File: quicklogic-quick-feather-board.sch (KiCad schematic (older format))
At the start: 28 parts, among them IC1 EOS-S3, J5 0473460001, U1 TPS62821DLCR, U2 MCP73831T-2ACI_OT, U3 MX25U6435FZNI-10G, X1 ECS-_327-12_5-34B-TR

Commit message: Changed flash memory, connected missing nets, cleanup
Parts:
- removed R9: R_10k_0402, antmicro-footprints:0402-res, symbol antmicroResistors0402:R_10k_0402
- removed U3: MX25U6435FZNI-10G, antmicro-footprints:DFN-8-1EP_6x5mm_P1.27mm_EP4x3.4mm, symbol quicklogic-quick-feather-board-rescue:MX25U6435FZNI-10G-antmicroMemory
- added R11, R7: R_22R_0402, antmicro-footprints:0402-res, symbol antmicroResistors0402:R_22R_0402
- added R12: R_10k_0402, antmicro-footprints:0402-res, symbol antmicroResistors0402:R_10k_0402
- added R9: R_1k5_0402, antmicro-footprints:0402-res, symbol antmicroResistors0402:R_1k5_0402
- added U3: GD25Q16CWIGR, antmicro-footprints:GD25Q16CWIG, symbol antmicroMemory:GD25Q16CWIGR
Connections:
- net labels added: PU_CTRL_USBP, SPI_HOLD, SPI_WP
- net labels removed: 1V8_SYS, EOS_VDD, IO23, IO28, IO29, SPI_MASTER_MISO, SPI_MASTER_MOSI, SPI_MASTER_SCK, SPI_MASTER_SS
- wire segments 110 -> 119
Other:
- note added: "Battery charger"
- note added: "EOS S3 FPGA"
- note added: "Flash memory"
- note added: "Supply"
- note added: "USB"
- note added: "Within same package this Flash can be replaced with \n64Mb one (GD25Q64CWIGR)"
- note removed: "TODO: connect SPI flash, add voltage level shifting if necessary (and pullups)"
- note removed: "TODO: connect to power supply source"
- note removed: "TODO: decide if we want to have 1v8 or 3v3 power supply for EOS (flash requires 1v8)"
- moved on the sheet: C1, C2, C3, C4, C5, C6, C7, D1, D2, J5, L1, R1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

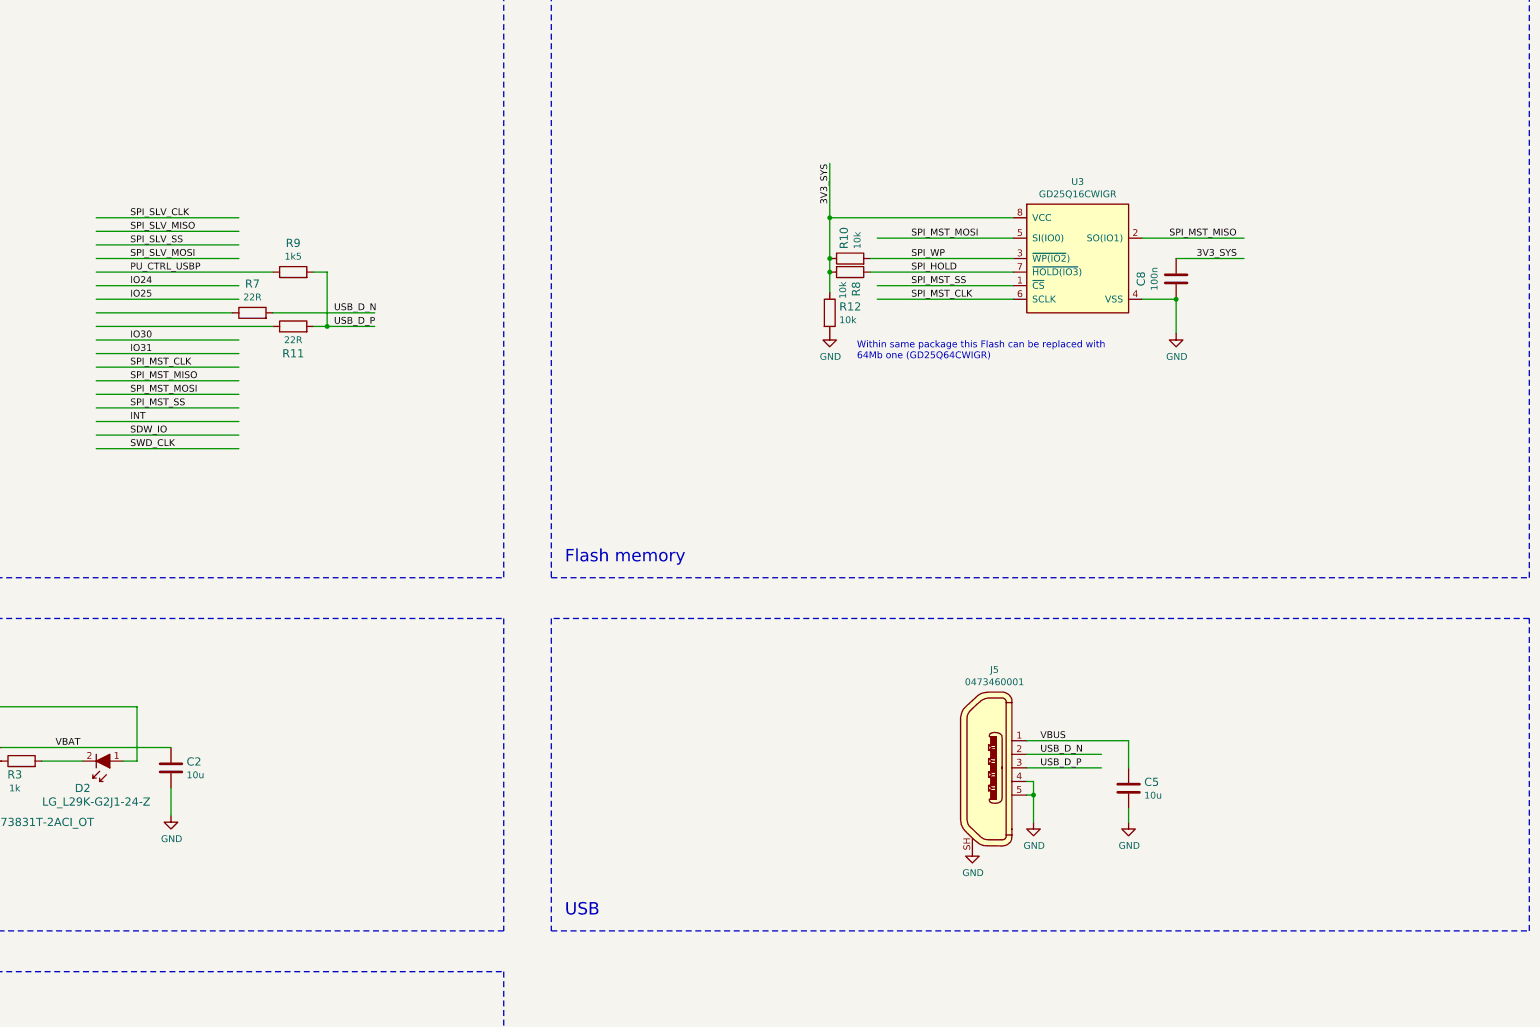
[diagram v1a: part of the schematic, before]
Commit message: Added IM69D130 microphone to schematics
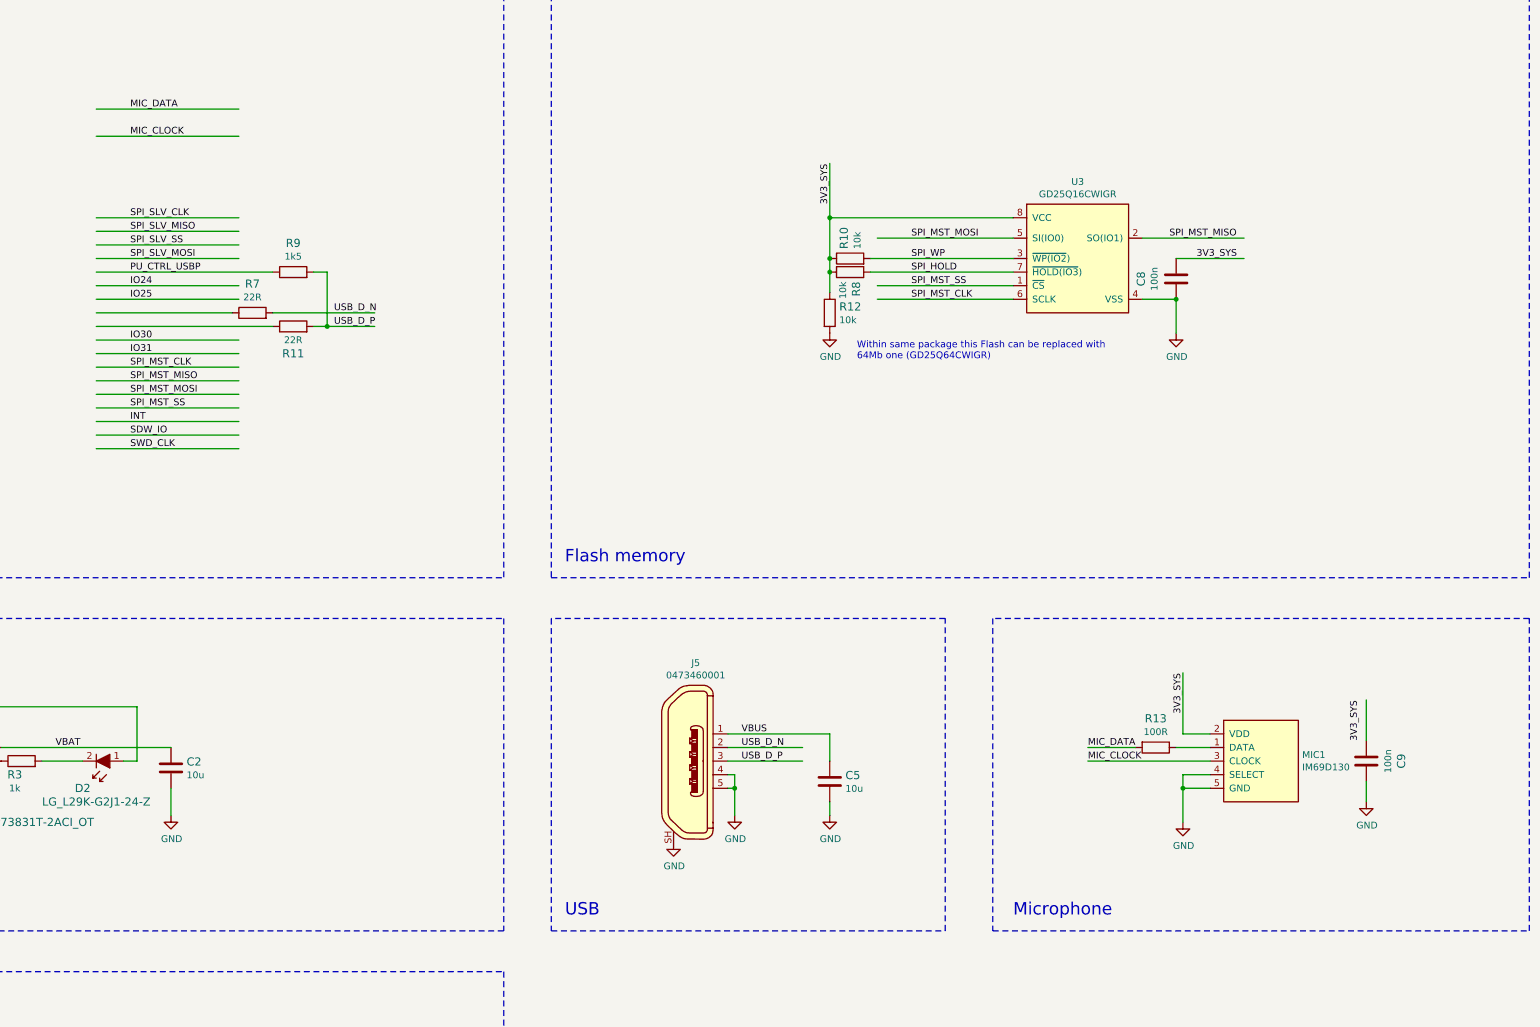
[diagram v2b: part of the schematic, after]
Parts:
- added C9: C_100n_0402_6V3, antmicro-footprints:0402-cap, symbol antmicroCapacitors0402:C_100n_0402_6V3
- added MIC1: IM69D130, antmicro-footprints:IM69D130, symbol antmicroMicrophones:IM69D130
- added R13: R_100R_0402, antmicro-footprints:0402-res, symbol antmicroResistors0402:R_100R_0402
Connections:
- net labels added: MIC_CLOCK, MIC_DATA
- wire segments 119 -> 132
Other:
- note added: "Microphone"
- moved on the sheet: C5, J5
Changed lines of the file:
@@
 L antmicroUSBDVIHDMIConnectors:0473460001 J5
 U 1 1 5DB1F3A2
-P 11800 6600
-F 0 "J5" H 11863 7323 50  0000 C CNN
-F 1 "0473460001" H 11863 7232 50  0000 C CNN
-F 2 "antmicro-footprints:USB_Micro_B_Female_0473460001" H 12000 6800 60  0001 L CNN
-F 3 "https://www.molex.com/pdm_docs/sd/473460001_sd.pdf" H 12000 6900 60  0001 L CNN
-F 4 "0473460001" H 12000 7100 60  0001 L CNN "MPN"
-F 5 "Molex" H 12000 7700 60  0001 L CNN "Manufacturer"
-	1    11800 6600
-	1    0    0    -1
-$EndComp
-Wire Wire Line
-	12100 6500 12650 6500
-Wire Wire Line
-	12100 6600 12650 6600
-Wire Wire Line
-	12100 6700 12150 6700
-Wire Wire Line
-	12150 6700 12150 6800
-Wire Wire Line
-	12150 6800 12100 6800
-Wire Wire Line
-	12150 6800 12150 7000
+P 9600 6550
+F 0 "J5" H 9663 7273 50  0000 C CNN
+F 1 "0473460001" H 9663 7182 50  0000 C CNN
+F 2 "antmicro-footprints:USB_Micro_B_Female_0473460001" H 9800 6750 60  0001 L CNN
+F 3 "https://www.molex.com/pdm_docs/sd/473460001_sd.pdf" H 9800 6850 60  0001 L CNN
+F 4 "0473460001" H 9800 7050 60  0001 L CNN "MPN"
+F 5 "Molex" H 9800 7650 60  0001 L CNN "Manufacturer"
+	1    9600 6550
+	1    0    0    -1
+$EndComp
+Wire Wire Line
+	9900 6450 10450 6450
+Wire Wire Line
+	9900 6550 10450 6550
+Wire Wire Line
+	9900 6650 9950 6650
+Wire Wire Line
+	9950 6650 9950 6750
+Wire Wire Line
+	9950 6750 9900 6750
+Wire Wire Line
+	9950 6750 9950 6950
 $Comp
 L power:GND #PWR011
 U 1 1 5DCF0111
-P 12150 7000
-F 0 "#PWR011" H 12150 6750 50  0001 C CNN
-F 1 "GND" H 12155 6827 50  0000 C CNN
-F 2 "" H 12150 7000 50  0001 C CNN
-F 3 "" H 12150 7000 50  0001 C CNN
-	1    12150 7000
-	1    0    0    -1
-$EndComp
-Text Label 12200 6400 0    50   ~ 0
+P 9950 6950
+F 0 "#PWR011" H 9950 6700 50  0001 C CNN
+F 1 "GND" H 9955 6777 50  0000 C CNN
+F 2 "" H 9950 6950 50  0001 C CNN
+F 3 "" H 9950 6950 50  0001 C CNN
+	1    9950 6950
+	1    0    0    -1
+$EndComp
+Text Label 10000 6350 0    50   ~ 0
 VBUS
-Text Label 12200 6600 0    50   ~ 0
+Text Label 10000 6550 0    50   ~ 0
 USB_D_P
-Text Label 12200 6500 0    50   ~ 0
+Text Label 10000 6450 0    50   ~ 0
 USB_D_N
-Connection ~ 12150 6800
+Connection ~ 9950 6750
 $Comp
 L power:GND #PWR0101
 U 1 1 5DE8E3C8
-P 11700 7200
-F 0 "#PWR0101" H 11700 6950 50  0001 C CNN
-F 1 "GND" H 11705 7027 50  0000 C CNN
-F 2 "" H 11700 7200 50  0001 C CNN
-F 3 "" H 11700 7200 50  0001 C CNN
-	1    11700 7200
+P 9500 7150
+F 0 "#PWR0101" H 9500 6900 50  0001 C CNN
+F 1 "GND" H 9505 6977 50  0000 C CNN
+F 2 "" H 9500 7150 50  0001 C CNN
+F 3 "" H 9500 7150 50  0001 C CNN
+	1    9500 7150
 	1    0    0    -1
 $EndComp
@@
 L antmicroCapacitors0603:C_10u_0603 C5
 U 1 1 5DC240D8
-P 12850 6750
-F 0 "C5" H 12965 6795 60  0000 L CNN
-F 1 "C_10u_0603" H 12850 6600 60  0001 C CNN
-F 2 "antmicro-footprints:0603-cap" H 13050 6950 60  0001 L CNN
-F 3 "" H 12850 6750 50  0001 C CNN
-F 4 "AVX" H 13050 7150 60  0001 L CNN "Manufacturer"
-F 5 "06036D106MAT2A" H 13050 7050 60  0001 L CNN "MPN"
-F 6 "10u" H 12965 6697 50  0000 L CNN "Val"
-	1    12850 6750
-	1    0    0    -1
-$EndComp
-Wire Wire Line
-	12850 6400 12850 6600
-Wire Wire Line
-	12100 6400 12850 6400
+P 10650 6700
+F 0 "C5" H 10765 6745 60  0000 L CNN
+F 1 "C_10u_0603" H 10650 6550 60  0001 C CNN
+F 2 "antmicro-footprints:0603-cap" H 10850 6900 60  0001 L CNN
+F 3 "" H 10650 6700 50  0001 C CNN
+F 4 "AVX" H 10850 7100 60  0001 L CNN "Manufacturer"
+F 5 "06036D106MAT2A" H 10850 7000 60  0001 L CNN "MPN"
+F 6 "10u" H 10765 6647 50  0000 L CNN "Val"
+	1    10650 6700
+	1    0    0    -1
+$EndComp
+Wire Wire Line
+	10650 6350 10650 6550
+Wire Wire Line
+	9900 6350 10650 6350
 $Comp
 L power:GND #PWR0109
 U 1 1 5DC24A74
-P 12850 7000
-F 0 "#PWR0109" H 12850 6750 50  0001 C CNN
-F 1 "GND" H 12855 6827 50  0000 C CNN
-F 2 "" H 12850 7000 50  0001 C CNN
-F 3 "" H 12850 7000 50  0001 C CNN
-	1    12850 7000
-	1    0    0    -1
-$EndComp
-Wire Wire Line
-	12850 6900 12850 7000
+P 10650 6950
+F 0 "#PWR0109" H 10650 6700 50  0001 C CNN
+F 1 "GND" H 10655 6777 50  0000 C CNN
+F 2 "" H 10650 6950 50  0001 C CNN
+F 3 "" H 10650 6950 50  0001 C CNN
+	1    10650 6950
+	1    0    0    -1
+$EndComp
+Wire Wire Line
+	10650 6850 10650 6950
 $Comp
 L antmicroDiodesRectifiersSingle:MBR0520LT1G D1
@@
 	8600 5500 8600 7800
 Wire Notes Line
-	8600 7800 15800 7800
-Wire Notes Line
-	15800 7800 15800 5500
-Wire Notes Line
-	15800 5500 8600 5500
+	8600 7800 11500 7800
+Wire Notes Line
+	11500 7800 11500 5500
+Wire Notes Line
+	11500 5500 8600 5500
 Text Label 2200 1550 0    50   ~ 0
 3V3_SYS
@@
 Text Notes 8700 7700 0    91   ~ 0
 USB
+Wire Notes Line
+	11850 5500 11850 7800
+Wire Notes Line
+	11850 7800 15800 7800
+Wire Notes Line
+	15800 7800 15800 5500
+Wire Notes Line
+	15800 5500 11850 5500
+$Comp
+L antmicroMicrophones:IM69D130 MIC1
+U 1 1 5DDA20C5
+P 13550 6250
+F 0 "MIC1" H 14128 5996 50  0000 L CNN
+F 1 "IM69D130" H 14128 5905 50  0000 L CNN
+F 2 "antmicro-footprints:IM69D130" H 13550 6300 50  0001 C CNN
+F 3 "https://www.infineon.com/dgdl/Infineon-IM69D130-DS-v01_00-EN.pdf?fileId=5546d462602a9dc801607a0e46511a2e" H 14000 5600 50  0001 C CNN
+	1    13550 6250
+	1    0    0    -1
+$EndComp
+Wire Wire Line
+	13450 6350 13250 6350
+Wire Wire Line
+	13250 6350 13250 5900
+Wire Wire Line
+	13450 6750 13250 6750
+Wire Wire Line
+	13250 6750 13250 7000
+$Comp
+L power:GND #PWR04
+U 1 1 5DDAB4E6
+P 13250 7000
+F 0 "#PWR04" H 13250 6750 50  0001 C CNN
+F 1 "GND" H 13255 6827 50  0000 C CNN
+F 2 "" H 13250 7000 50  0001 C CNN
+F 3 "" H 13250 7000 50  0001 C CNN
+	1    13250 7000
+	1    0    0    -1
+$EndComp
+Wire Wire Line
+	13450 6450 13200 6450
+Wire Wire Line
+	13450 6550 12550 6550
+Wire Wire Line
+	13450 6650 13250 6650
+$Comp
+L antmicroResistors0402:R_100R_0402 R13
+U 1 1 5DDB9D20
+P 13050 6450
+F 0 "R13" H 13050 6237 60  0000 C CNN
+F 1 "R_100R_0402" H 13050 6300 60  0001 C CNN
+F 2 "antmicro-footprints:0402-res" H 13250 6650 60  0001 L CNN
+F 3 "" H 13050 6450 50  0001 C CNN
+F 4 "BOURNS" H 13250 6850 60  0001 L CNN "Manufacturer"
+F 5 "CR0402-FX-1000GLF" H 13250 6750 60  0001 L CNN "MPN"
+F 6 "100R" H 13050 6335 50  0000 C CNN "Val"
+	1    13050 6450
+	-1   0    0    1
+$EndComp
+Wire Wire Line
+	12900 6450 12550 6450
+Wire Wire Line
+	13250 6650 13250 6750
+Connection ~ 13250 6750
+Text Label 13250 6200 1    50   ~ 0
+3V3_SYS
+Text Label 12550 6450 0    50   ~ 0
+MIC_DATA
+Text Label 12550 6550 0    50   ~ 0
+MIC_CLOCK
+Text Notes 12000 7700 0    91   ~ 0
+Microphone
+$Comp
+L antmicroCapacitors0402:C_100n_0402_6V3 C9
+U 1 1 5DDE16B2
+P 14600 6550
+F 0 "C9" V 14342 6550 60  0000 C CNN
+F 1 "C_100n_0402_6V3" H 14600 6400 60  0001 C CNN
+F 2 "antmicro-footprints:0402-cap" H 14800 6750 60  0001 L CNN
+F 3 "" H 14600 6550 50  0001 C CNN
+F 4 "Walsin" H 14800 6950 60  0001 L CNN "Manufacturer"
+F 5 "0402X104K6R3CT" H 14800 6850 60  0001 L CNN "MPN"
+F 6 "100n" V 14440 6550 50  0000 C CNN "Val"
+	1    14600 6550
+	-1   0    0    1
+$EndComp
+Text Label 14550 6400 1    50   ~ 0
+3V3_SYS
+Wire Wire Line
+	14600 6100 14600 6400
+Wire Wire Line
+	14600 6700 14600 6850
+$Comp
+L power:GND #PWR05
+U 1 1 5DDF05E4
+P 14600 6850
+F 0 "#PWR05" H 14600 6600 50  0001 C CNN
+F 1 "GND" H 14605 6677 50  0000 C CNN
+F 2 "" H 14600 6850 50  0001 C CNN
+F 3 "" H 14600 6850 50  0001 C CNN
+	1    14600 6850
+	1    0    0    -1
+$EndComp
+Text Label 5500 1750 0    50   ~ 0
+MIC_DATA
+Text Label 5500 1950 0    50   ~ 0
+MIC_CLOCK
+Wire Wire Line
+	5250 1750 6300 1750
+Wire Wire Line
+	5250 1950 6300 1950
 $EndSCHEMATC

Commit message: Added TVS for USB
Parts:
- added D3: TPD2EUSB30DRTR, antmicro-footprints:SOT-3, symbol antmicroTVSDiodes:TPD2EUSB30DRTR
- U3: symbol antmicroMemory:GD25Q16CWIGR -> quicklogic-quick-feather-board-rescue:GD25Q16CWIGR-antmicroMemory
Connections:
- wire segments 132 -> 138
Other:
- moved on the sheet: C5, J5
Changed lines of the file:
@@
 EESchema Schematic File Version 4
 LIBS:quicklogic-quick-feather-board-cache
-EELAYER 26 0
+EELAYER 30 0
 EELAYER END
 $Descr A3 16535 11693
@@
 L antmicroUSBDVIHDMIConnectors:0473460001 J5
 U 1 1 5DB1F3A2
-P 9600 6550
-F 0 "J5" H 9663 7273 50  0000 C CNN
-F 1 "0473460001" H 9663 7182 50  0000 C CNN
-F 2 "antmicro-footprints:USB_Micro_B_Female_0473460001" H 9800 6750 60  0001 L CNN
-F 3 "https://www.molex.com/pdm_docs/sd/473460001_sd.pdf" H 9800 6850 60  0001 L CNN
-F 4 "0473460001" H 9800 7050 60  0001 L CNN "MPN"
-F 5 "Molex" H 9800 7650 60  0001 L CNN "Manufacturer"
-	1    9600 6550
-	1    0    0    -1
-$EndComp
-Wire Wire Line
-	9900 6450 10450 6450
-Wire Wire Line
-	9900 6550 10450 6550
-Wire Wire Line
-	9900 6650 9950 6650
-Wire Wire Line
-	9950 6650 9950 6750
-Wire Wire Line
-	9950 6750 9900 6750
-Wire Wire Line
-	9950 6750 9950 6950
+P 9000 6550
+F 0 "J5" H 9063 7273 50  0000 C CNN
+F 1 "0473460001" H 9063 7182 50  0000 C CNN
+F 2 "antmicro-footprints:USB_Micro_B_Female_0473460001" H 9200 6750 60  0001 L CNN
+F 3 "https://www.molex.com/pdm_docs/sd/473460001_sd.pdf" H 9200 6850 60  0001 L CNN
+F 4 "0473460001" H 9200 7050 60  0001 L CNN "MPN"
+F 5 "Molex" H 9200 7650 60  0001 L CNN "Manufacturer"
+	1    9000 6550
+	1    0    0    -1
+$EndComp
+Wire Wire Line
+	9300 6650 9350 6650
+Wire Wire Line
+	9350 6650 9350 6750
+Wire Wire Line
+	9350 6750 9300 6750
+Wire Wire Line
+	9350 6750 9350 6950
 $Comp
 L power:GND #PWR011
 U 1 1 5DCF0111
-P 9950 6950
-F 0 "#PWR011" H 9950 6700 50  0001 C CNN
-F 1 "GND" H 9955 6777 50  0000 C CNN
-F 2 "" H 9950 6950 50  0001 C CNN
-F 3 "" H 9950 6950 50  0001 C CNN
-	1    9950 6950
-	1    0    0    -1
-$EndComp
-Text Label 10000 6350 0    50   ~ 0
+P 9350 6950
+F 0 "#PWR011" H 9350 6700 50  0001 C CNN
+F 1 "GND" H 9355 6777 50  0000 C CNN
+F 2 "" H 9350 6950 50  0001 C CNN
+F 3 "" H 9350 6950 50  0001 C CNN
+	1    9350 6950
+	1    0    0    -1
+$EndComp
+Text Label 9400 6350 0    50   ~ 0
 VBUS
-Text Label 10000 6550 0    50   ~ 0
+Text Label 9400 6550 0    50   ~ 0
 USB_D_P
-Text Label 10000 6450 0    50   ~ 0
+Text Label 9400 6450 0    50   ~ 0
 USB_D_N
-Connection ~ 9950 6750
+Connection ~ 9350 6750
 $Comp
 L power:GND #PWR0101
 U 1 1 5DE8E3C8
-P 9500 7150
-F 0 "#PWR0101" H 9500 6900 50  0001 C CNN
-F 1 "GND" H 9505 6977 50  0000 C CNN
-F 2 "" H 9500 7150 50  0001 C CNN
-F 3 "" H 9500 7150 50  0001 C CNN
-	1    9500 7150
+P 8900 7150
+F 0 "#PWR0101" H 8900 6900 50  0001 C CNN
+F 1 "GND" H 8905 6977 50  0000 C CNN
+F 2 "" H 8900 7150 50  0001 C CNN
+F 3 "" H 8900 7150 50  0001 C CNN
+	1    8900 7150
 	1    0    0    -1
 $EndComp
@@
 L antmicroCapacitors0603:C_10u_0603 C5
 U 1 1 5DC240D8
-P 10650 6700
-F 0 "C5" H 10765 6745 60  0000 L CNN
-F 1 "C_10u_0603" H 10650 6550 60  0001 C CNN
-F 2 "antmicro-footprints:0603-cap" H 10850 6900 60  0001 L CNN
-F 3 "" H 10650 6700 50  0001 C CNN
-F 4 "AVX" H 10850 7100 60  0001 L CNN "Manufacturer"
-F 5 "06036D106MAT2A" H 10850 7000 60  0001 L CNN "MPN"
-F 6 "10u" H 10765 6647 50  0000 L CNN "Val"
-	1    10650 6700
-	1    0    0    -1
-$EndComp
-Wire Wire Line
-	10650 6350 10650 6550
-Wire Wire Line
-	9900 6350 10650 6350
-$Comp
-L power:GND #PWR0109
-U 1 1 5DC24A74
-P 10650 6950
-F 0 "#PWR0109" H 10650 6700 50  0001 C CNN
-F 1 "GND" H 10655 6777 50  0000 C CNN
-F 2 "" H 10650 6950 50  0001 C CNN
-F 3 "" H 10650 6950 50  0001 C CNN
-	1    10650 6950
-	1    0    0    -1
-$EndComp
-Wire Wire Line
-	10650 6850 10650 6950
+P 10050 6850
+F 0 "C5" H 10165 6895 60  0000 L CNN
+F 1 "C_10u_0603" H 10050 6700 60  0001 C CNN
+F 2 "antmicro-footprints:0603-cap" H 10250 7050 60  0001 L CNN
+F 3 "" H 10050 6850 50  0001 C CNN
+F 4 "AVX" H 10250 7250 60  0001 L CNN "Manufacturer"
+F 5 "06036D106MAT2A" H 10250 7150 60  0001 L CNN "MPN"
+F 6 "10u" H 10165 6797 50  0000 L CNN "Val"
+	1    10050 6850
+	1    0    0    -1
+$EndComp
+Wire Wire Line
+	9300 6350 10050 6350
 $Comp
 L antmicroDiodesRectifiersSingle:MBR0520LT1G D1
@@
 SPI_MST_CLK
 $Comp
-L antmicroMemory:GD25Q16CWIGR U3
+L quicklogic-quick-feather-board-rescue:GD25Q16CWIGR-antmicroMemory U3
 U 1 1 5DDDF93D
 P 12100 2450
@@
 Wire Notes Line
 	8600 5500 8600 7800
-Wire Notes Line
-	8600 7800 11500 7800
 Wire Notes Line
 	11500 7800 11500 5500
@@
 Wire Wire Line
 	5250 1950 6300 1950
+Wire Notes Line
+	8600 7800 11500 7800
+$Comp
+L antmicroTVSDiodes:TPD2EUSB30DRTR D3
+U 1 1 5DDCDC86
+P 10800 6550
+F 0 "D3" H 10800 6907 60  0000 C CNN
+F 1 "TPD2EUSB30DRTR" H 10800 6801 60  0000 C CNN
+F 2 "antmicro-footprints:SOT-3" H 11000 6750 60  0001 L CNN
+F 3 "http://www.ti.com/general/docs/suppproductinfo.tsp?distId=10&gotoUrl=http%3A%2F%2Fwww.ti.com%2Flit%2Fgpn%2Ftpd2eusb30" H 11000 6850 60  0001 L CNN
+F 4 "Texas Instruments" H 11000 7650 60  0001 L CNN "Manufacturer"
+F 5 "TPD2EUSB30DRTR" H 11000 7050 60  0001 L CNN "MPN"
+	1    10800 6550
+	-1   0    0    -1
+$EndComp
+Wire Wire Line
+	10050 7000 10050 7100
+$Comp
+L power:GND #PWR0109
+U 1 1 5DC24A74
+P 10050 7100
+F 0 "#PWR0109" H 10050 6850 50  0001 C CNN
+F 1 "GND" H 10055 6927 50  0000 C CNN
+F 2 "" H 10050 7100 50  0001 C CNN
+F 3 "" H 10050 7100 50  0001 C CNN
+	1    10050 7100
+	1    0    0    -1
+$EndComp
+Wire Wire Line
+	9300 6550 10500 6550
+Wire Wire Line
+	10050 6350 10050 6700
+Wire Wire Line
+	11100 6550 11250 6550
+Wire Wire Line
+	11250 6550 11250 6100
+Wire Wire Line
+	11250 6100 10250 6100
+Wire Wire Line
+	10250 6100 10250 6450
+Wire Wire Line
+	9300 6450 10250 6450
+Wire Wire Line
+	10800 6850 10800 7000
+Wire Wire Line
+	10800 7000 10050 7000
+Connection ~ 10050 7000
 $EndSCHEMATC

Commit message: Updated library connections
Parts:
- IC1: symbol quicklogic-quick-feather-board-rescue:EOS-S3-antmicroBGAchips -> antmicroBGAchips:EOS-S3
- U3: symbol quicklogic-quick-feather-board-rescue:GD25Q16CWIGR-antmicroMemory -> antmicroMemory:GD25Q16CWIGR
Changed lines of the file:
@@
 $EndComp
 $Comp
-L quicklogic-quick-feather-board-rescue:EOS-S3-antmicroBGAchips IC1
+L antmicroBGAchips:EOS-S3 IC1
 U 1 1 5DCF18DD
 P 3300 1400
@@
 SPI_MST_CLK
 $Comp
-L quicklogic-quick-feather-board-rescue:GD25Q16CWIGR-antmicroMemory U3
+L antmicroMemory:GD25Q16CWIGR U3
 U 1 1 5DDDF93D
 P 12100 2450
